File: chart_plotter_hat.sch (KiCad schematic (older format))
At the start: 66 parts, among them J1 JST PH, J10 JST PH, J2 JST PH, J3 40HAT, J4 JST PH, J5 JST PH, J6 JST PH, J7 JST PH, J8 Conn_02x03_Odd_Even, J9 JST PH, Q1 DMG2305UX, Q2 DMMT5401, U1 ATmega328P-AU, U10 DCP01B, U11 VCAN26A2, U2 CAT24C32, U3 MPM3610-5.0-adafruit, U4 LT1762-3.3, U5 G3VM-201FR, U6 MCP2515-xSO, U7 MCP2551-I-SN, U8 LT1762-MS8, U9 ADuM1201BR, Y1 16MHz

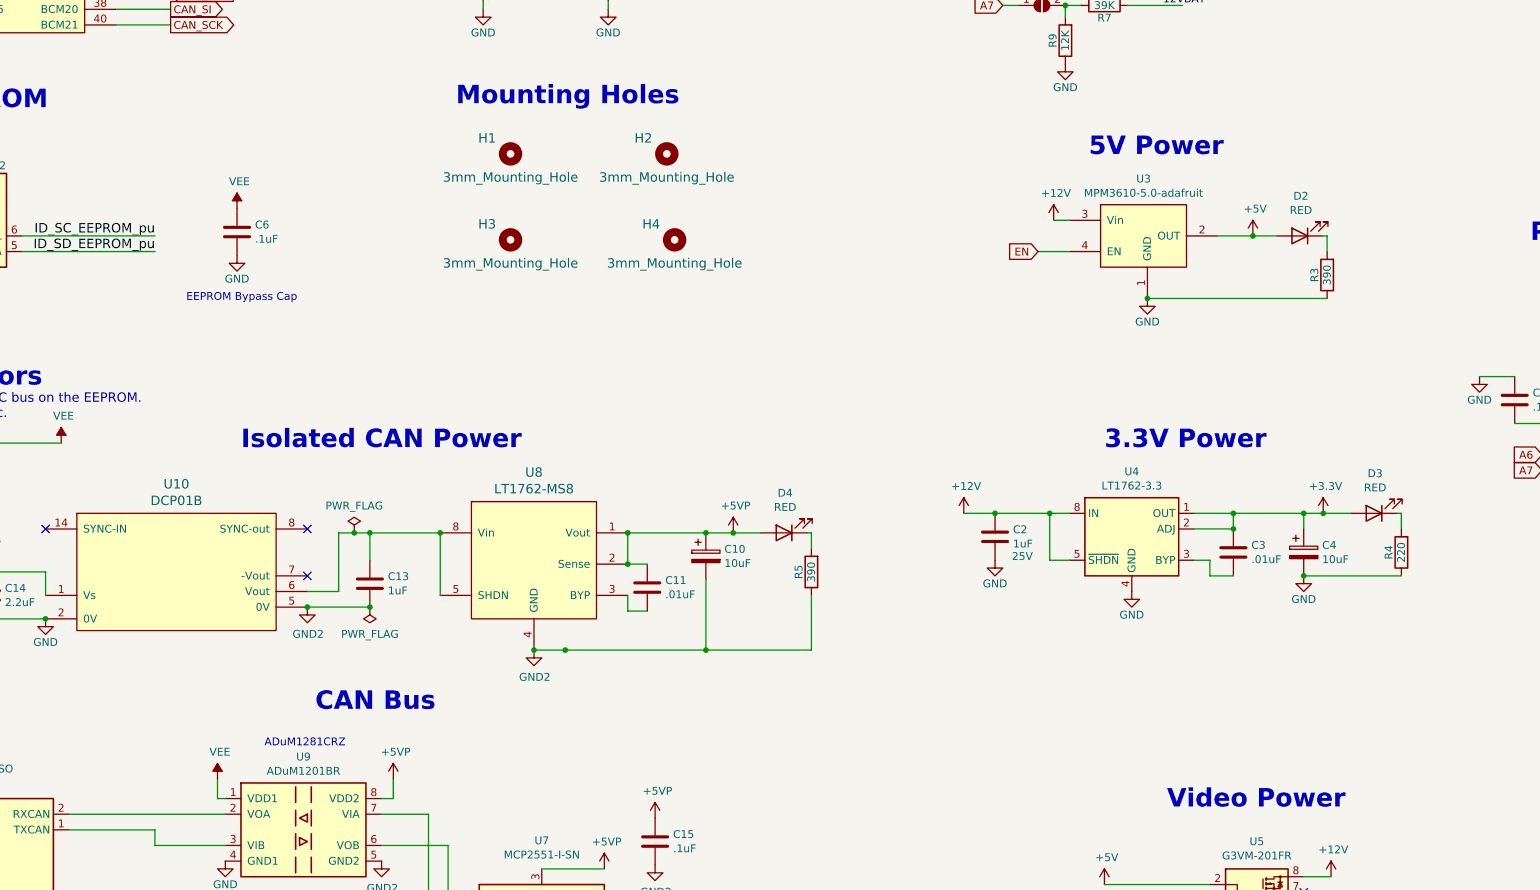
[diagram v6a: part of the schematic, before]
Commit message: Added DS1307 RTC
Added coin cell battery holder
updated bom
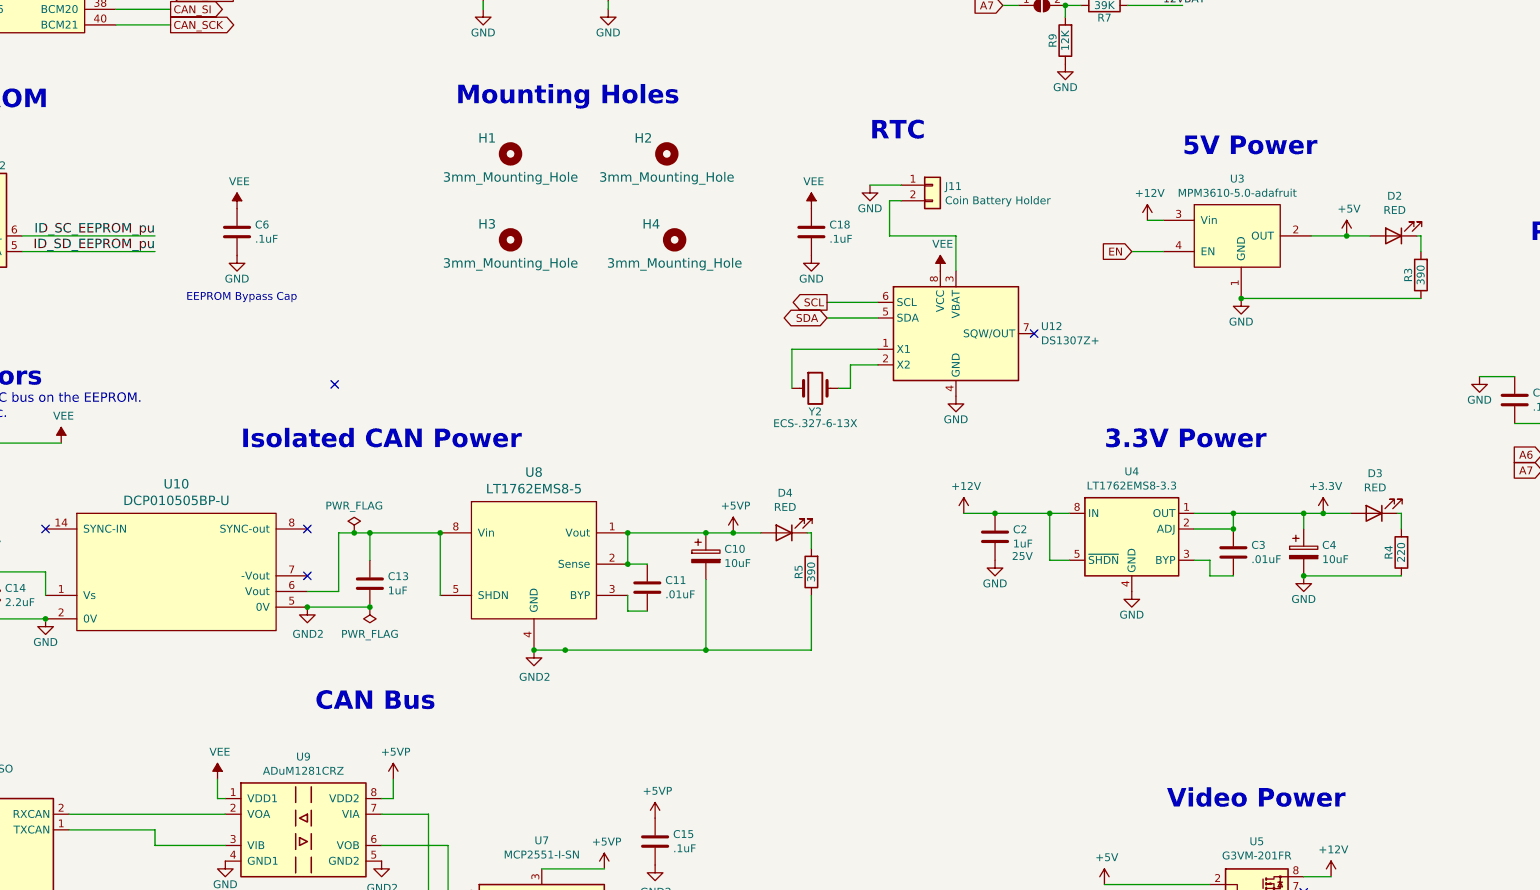
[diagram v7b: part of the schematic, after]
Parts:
- added C18: .1uF, Capacitors_SMD:C_0603, symbol Device:C
- added J11: Coin Battery Holder, geda:3001, symbol Connector_Generic:Conn_01x02
- added U12: DS1307Z+, Housings_SOIC:SOIC-8_3.9x4.9mm_Pitch1.27mm, symbol Timer_RTC:DS1307Z+
- added Y2: ECS-.327-6-13X, Crystals:Crystal_Round_d2.0mm_Vertical, symbol Device:Crystal
- U10: value DCP01B -> DCP010505BP-U
- U4: value LT1762-3.3 -> LT1762EMS8-3.3
- U8: value LT1762-MS8 -> LT1762EMS8-5
- U9: value ADuM1201BR -> ADuM1281CRZ
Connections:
- net GND: now also C18.2, J11.1 (Pin_1), U12.4 (GND)
- net SCL: now also U12.6 (SCL)
- net SDA: now also U12.5 (SDA)
- net VEE: now also C18.1, U12.8 (VCC)
- new net: U12.1 (X1), Y2.1
- new net: U12.2 (X2), Y2.2
- new net: J11.2 (Pin_2), U12.3 (VBAT)
- no-connect marks 25 -> 27
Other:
- note added: "RTC"
- note removed: "ADuM1281CRZ"
- moved on the sheet: D2, R3, U3
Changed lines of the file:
@@
 Power Connector
 Wire Wire Line
-	9250 4425 9350 4425
-Text GLabel 9150 4625 0    50   Input ~ 0
+	9850 4425 9950 4425
+Text GLabel 9750 4625 0    50   Input ~ 0
 EN
 Text GLabel 13950 7825 2    50   Output ~ 0
@@
 L power:+12V #PWR016
 U 1 1 5FDF51C8
-P 9250 4425
-F 0 "#PWR016" H 9250 4275 50  0001 C CNN
-F 1 "+12V" H 9265 4598 50  0000 C CNN
-F 2 "" H 9250 4425 50  0001 C CNN
-F 3 "" H 9250 4425 50  0001 C CNN
-	1    9250 4425
+P 9850 4425
+F 0 "#PWR016" H 9850 4275 50  0001 C CNN
+F 1 "+12V" H 9865 4598 50  0000 C CNN
+F 2 "" H 9850 4425 50  0001 C CNN
+F 3 "" H 9850 4425 50  0001 C CNN
+	1    9850 4425
 	1    0    0    -1
 $EndComp
@@
 P 9750 6500
 F 0 "U4" H 9750 6967 50  0000 C CNN
-F 1 "LT1762-3.3" H 9750 6876 50  0000 C CNN
+F 1 "LT1762EMS8-3.3" H 9750 6876 50  0000 C CNN
 F 2 "Housings_SSOP:MSOP-8_3x3mm_Pitch0.65mm" H 9750 6150 50  0001 C CNN
 F 3 "https://www.analog.com/media/en/technical-documentation/data-sheets/LT1762.pdf" H 9750 5950 50  0001 C CNN
@@
 L power:GND #PWR0105
 U 1 1 5FD9629F
-P 9850 4925
-F 0 "#PWR0105" H 9850 4675 50  0001 C CNN
-F 1 "GND" H 9850 4775 50  0000 C CNN
-F 2 "" H 9850 4925 50  0000 C CNN
-F 3 "" H 9850 4925 50  0000 C CNN
-	1    9850 4925
+P 10450 4925
+F 0 "#PWR0105" H 10450 4675 50  0001 C CNN
+F 1 "GND" H 10450 4775 50  0000 C CNN
+F 2 "" H 10450 4925 50  0000 C CNN
+F 3 "" H 10450 4925 50  0000 C CNN
+	1    10450 4925
 	1    0    0    -1
 $EndComp
@@
 Text Notes 9575 5900 0    118  ~ 24
 3.3V Power
-Text Notes 9475 4025 0    118  ~ 24
+Text Notes 10075 4025 0    118  ~ 24
 5V Power
 Text Notes 12300 4575 0    118  ~ 24
@@
 L adafruit:MPM3610-adafruit U3
 U 1 1 5FD6743F
-P 9850 4275
-F 0 "U3" H 9825 4390 50  0000 C CNN
-F 1 "MPM3610-5.0-adafruit" H 9825 4299 50  0000 C CNN
-F 2 "CustomComponents:Adafruit_MPM3610" H 9850 4275 50  0001 C CNN
-F 3 "" H 9850 4275 50  0001 C CNN
-	1    9850 4275
-	1    0    0    -1
-$EndComp
-Wire Wire Line
-	9150 4625 9350 4625
+P 10450 4275
+F 0 "U3" H 10425 4390 50  0000 C CNN
+F 1 "MPM3610-5.0-adafruit" H 10425 4299 50  0000 C CNN
+F 2 "CustomComponents:Adafruit_MPM3610" H 10450 4275 50  0001 C CNN
+F 3 "" H 10450 4275 50  0001 C CNN
+	1    10450 4275
+	1    0    0    -1
+$EndComp
+Wire Wire Line
+	9750 4625 9950 4625
 $Comp
 L CustomComponents:G3VM-201FR U5
@@
 L power:+5V #PWR0121
 U 1 1 600ECE9F
-P 10525 4525
-F 0 "#PWR0121" H 10525 4375 50  0001 C CNN
-F 1 "+5V" H 10540 4698 50  0000 C CNN
-F 2 "" H 10525 4525 50  0001 C CNN
-F 3 "" H 10525 4525 50  0001 C CNN
-	1    10525 4525
+P 11125 4525
+F 0 "#PWR0121" H 11125 4375 50  0001 C CNN
+F 1 "+5V" H 11140 4698 50  0000 C CNN
+F 2 "" H 11125 4525 50  0001 C CNN
+F 3 "" H 11125 4525 50  0001 C CNN
+	1    11125 4525
 	1    0    0    -1
 $EndComp
@@
 P 4450 8325
 F 0 "U9" H 4450 8792 50  0000 C CNN
-F 1 "ADuM1201BR" H 4450 8701 50  0000 C CNN
+F 1 "ADuM1281CRZ" H 4450 8701 50  0000 C CNN
 F 2 "Housings_SOIC:SOIC-8_3.9x4.9mm_Pitch1.27mm" H 4450 7925 50  0001 C CIN
 F 3 "https://www.analog.com/static/imported-files/data_sheets/ADuM1200_1201.pdf" H 4450 8225 50  0001 C CNN
@@
 	15100 4900 15425 4900
 Wire Wire Line
-	10300 4525 10525 4525
+	10900 4525 11125 4525
 NoConn ~ 15575 1275
 Text GLabel 3275 9425 2    50   Input ~ 0
@@
 P 5925 6625
 F 0 "U8" H 5925 7212 60  0000 C CNN
-F 1 "LT1762-MS8" H 5925 7106 60  0000 C CNN
+F 1 "LT1762EMS8-5" H 5925 7106 60  0000 C CNN
 F 2 "Housings_SSOP:MSOP-8_3x3mm_Pitch0.65mm" H 5925 6625 60  0001 C CNN
 F 3 "" H 5925 6625 60  0001 C CNN
@@
 P 3625 6700
 F 0 "U10" H 3637 7287 60  0000 C CNN
-F 1 "DCP01B" H 3637 7181 60  0000 C CNN
+F 1 "DCP010505BP-U" H 3637 7181 60  0000 C CNN
 F 2 "CustomComponents:DCP01B_SO_7_14" H 3650 6700 60  0001 C CNN
 F 3 "" H 3650 6700 60  0001 C CNN
@@
 L Device:R R3
 U 1 1 616854F3
-P 11000 4775
-F 0 "R3" V 11080 4775 50  0000 C CNN
-F 1 "390" V 11000 4775 50  0000 C CNN
-F 2 "Resistors_SMD:R_0603" V 10930 4775 50  0001 C CNN
-F 3 "" H 11000 4775 50  0001 C CNN
-	1    11000 4775
+P 11600 4775
+F 0 "R3" V 11680 4775 50  0000 C CNN
+F 1 "390" V 11600 4775 50  0000 C CNN
+F 2 "Resistors_SMD:R_0603" V 11530 4775 50  0001 C CNN
+F 3 "" H 11600 4775 50  0001 C CNN
+	1    11600 4775
 	-1   0    0    1
 $EndComp
@@
 L Device:LED D2
 U 1 1 616837C9
-P 10825 4525
-F 0 "D2" H 10818 4270 50  0000 C CNN
-F 1 "RED" H 10818 4361 50  0000 C CNN
-F 2 "Diodes_SMD:D_0603" H 10825 4525 50  0001 C CNN
-F 3 "~" H 10825 4525 50  0001 C CNN
-	1    10825 4525
+P 11425 4525
+F 0 "D2" H 11418 4270 50  0000 C CNN
+F 1 "RED" H 11418 4361 50  0000 C CNN
+F 2 "Diodes_SMD:D_0603" H 11425 4525 50  0001 C CNN
+F 3 "~" H 11425 4525 50  0001 C CNN
+	1    11425 4525
 	-1   0    0    1
 $EndComp
@@
 $EndComp
 Wire Wire Line
-	10525 4525 10675 4525
-Connection ~ 10525 4525
-Wire Wire Line
-	10975 4525 11000 4525
-Wire Wire Line
-	11000 4525 11000 4625
-Wire Wire Line
-	11000 4925 9850 4925
-Connection ~ 9850 4925
+	11125 4525 11275 4525
+Connection ~ 11125 4525
+Wire Wire Line
+	11575 4525 11600 4525
+Wire Wire Line
+	11600 4525 11600 4625
+Wire Wire Line
+	11600 4925 10450 4925
+Connection ~ 10450 4925
 Wire Wire Line
 	10975 6300 11150 6300
@@
 Wire Wire Line
 	1600 8425 1750 8425
-Text Notes 4200 7800 0    50   ~ 0
-ADuM1281CRZ
 Connection ~ 2425 6675
 Connection ~ 6125 7175
@@
 	6125 7175 7025 7175
 Connection ~ 5925 7175
+$Comp
+L Timer_RTC:DS1307Z+ U12
+U 1 1 6144E9CC
+P 8625 5150
+F 0 "U12" H 9169 5196 50  0000 L CNN
+F 1 "DS1307Z+" H 9169 5105 50  0000 L CNN
+F 2 "Housings_SOIC:SOIC-8_3.9x4.9mm_Pitch1.27mm" H 8625 4650 50  0001 C CNN
+F 3 "https://datasheets.maximintegrated.com/en/ds/DS1307.pdf" H 8625 5150 50  0001 C CNN
+	1    8625 5150
+	1    0    0    -1
+$EndComp
+Wire Wire Line
+	8125 4950 7800 4950
+Wire Wire Line
+	8125 5050 7800 5050
+$Comp
+L power:VEE #PWR037
+U 1 1 6149D61D
+P 8525 4750
+F 0 "#PWR037" H 8525 4600 50  0001 C CNN
+F 1 "VEE" H 8540 4923 50  0000 C CNN
+F 2 "" H 8525 4750 50  0001 C CNN
+F 3 "" H 8525 4750 50  0001 C CNN
+	1    8525 4750
+	1    0    0    -1
+$EndComp
+$Comp
+L power:GND #PWR038
+U 1 1 614A02FA
+P 8625 5550
+F 0 "#PWR038" H 8625 5300 50  0001 C CNN
+F 1 "GND" H 8625 5400 50  0000 C CNN
+F 2 "" H 8625 5550 50  0000 C CNN
+F 3 "" H 8625 5550 50  0000 C CNN
+	1    8625 5550
+	1    0    0    -1
+$EndComp
+$Comp
+L Connector_Generic:Conn_01x02 J11
+U 1 1 614A429A
+P 8475 4200
+F 0 "J11" H 8555 4192 50  0000 L CNN
+F 1 "Coin Battery Holder" H 8555 4101 50  0000 L CNN
+F 2 "geda:3001" H 8475 4200 50  0001 C CNN
+F 3 "~" H 8475 4200 50  0001 C CNN
+	1    8475 4200
+	1    0    0    -1
+$EndComp
+$Comp
+L power:GND #PWR036
+U 1 1 614F655A
+P 8075 4200
+F 0 "#PWR036" H 8075 3950 50  0001 C CNN
+F 1 "GND" H 8075 4050 50  0000 C CNN
+F 2 "" H 8075 4200 50  0000 C CNN
+F 3 "" H 8075 4200 50  0000 C CNN
+	1    8075 4200
+	1    0    0    -1
+$EndComp
+Wire Wire Line
+	8625 4525 8625 4750
+$Comp
+L Device:Crystal Y2
+U 1 1 6150DAC1
+P 7725 5500
+F 0 "Y2" H 7725 5350 50  0000 C CNN
+F 1 "ECS-.327-6-13X" H 7725 5275 50  0000 C CNN
+F 2 "Crystals:Crystal_Round_d2.0mm_Vertical" H 7725 5500 50  0001 C CNN
+F 3 "~" H 7725 5500 50  0001 C CNN
+	1    7725 5500
+	1    0    0    -1
+$EndComp
+Wire Wire Line
+	7875 5500 7950 5500
+Wire Wire Line
+	7950 5500 7950 5350
+Wire Wire Line
+	7950 5350 8125 5350
+Wire Wire Line
+	7575 5500 7575 5250
+NoConn ~ 9125 5150
+NoConn ~ 4650 5475
+Text GLabel 7800 5050 0    50   BiDi ~ 0
+SDA
+Text GLabel 7800 4950 0    50   Output ~ 0
+SCL
+Wire Wire Line
+	7575 5250 8125 5250
+Wire Wire Line
+	8075 4200 8275 4200
+Wire Wire Line
+	8625 4525 8200 4525
+Wire Wire Line
+	8200 4525 8200 4300
+Wire Wire Line
+	8200 4300 8275 4300
+$Comp
+L Device:C C18
+U 1 1 614B5FFD
+P 7700 4500
+F 0 "C18" H 7815 4546 50  0000 L CNN
+F 1 ".1uF" H 7815 4455 50  0000 L CNN
+F 2 "Capacitors_SMD:C_0603" H 7738 4350 50  0001 C CNN
+F 3 "~" H 7700 4500 50  0001 C CNN
+	1    7700 4500
+	1    0    0    -1
+$EndComp
+$Comp
+L power:GND #PWR042
+U 1 1 614D209C
+P 7700 4650
+F 0 "#PWR042" H 7700 4400 50  0001 C CNN
+F 1 "GND" H 7700 4500 50  0000 C CNN
+F 2 "" H 7700 4650 50  0000 C CNN
+F 3 "" H 7700 4650 50  0000 C CNN
+	1    7700 4650
+	1    0    0    -1
+$EndComp
+$Comp
+L power:VEE #PWR0110
+U 1 1 6151C438
+P 7700 4350
+F 0 "#PWR0110" H 7700 4200 50  0001 C CNN
+F 1 "VEE" H 7715 4523 50  0000 C CNN
+F 2 "" H 7700 4350 50  0001 C CNN
+F 3 "" H 7700 4350 50  0001 C CNN
+	1    7700 4350
+	1    0    0    -1
+$EndComp
+Text Notes 8075 3925 0    118  ~ 24
+RTC
 $EndSCHEMATC

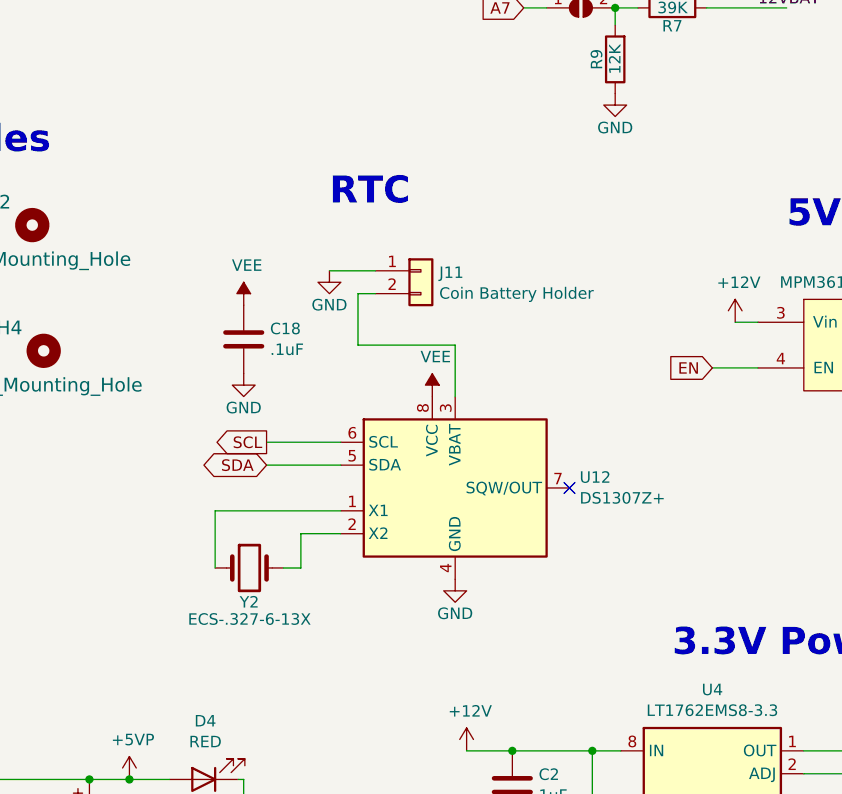
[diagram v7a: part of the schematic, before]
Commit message: Removed DS1307, (Not avail), added STEMMA QT conx
can connect an adafruit breakout board for RTC instead
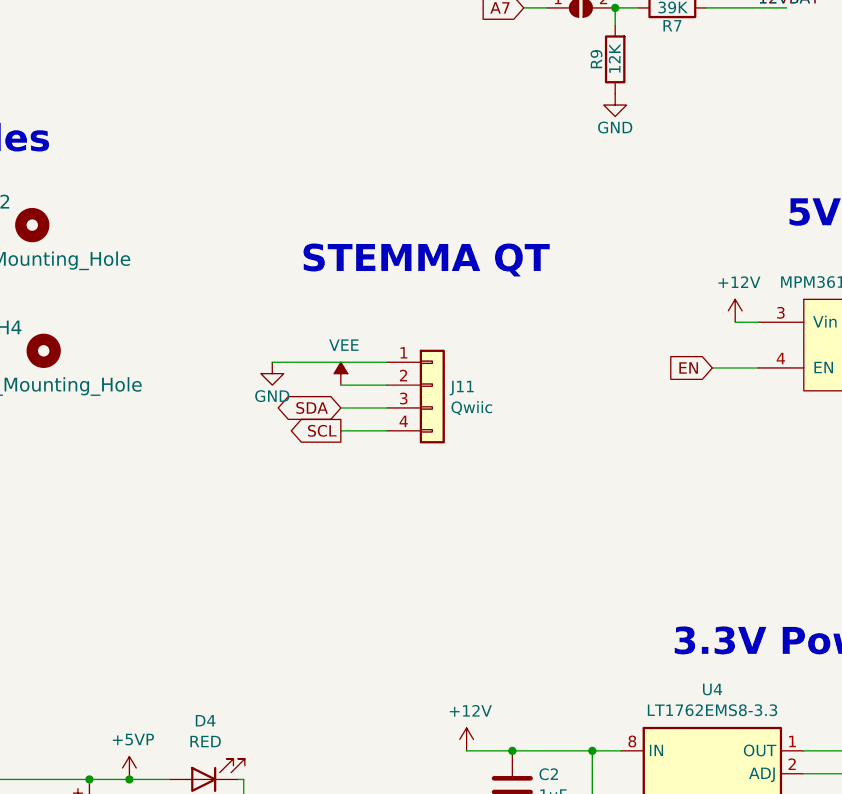
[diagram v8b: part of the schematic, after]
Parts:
- removed C18: .1uF, Capacitors_SMD:C_0603, symbol Device:C
- removed J11: Coin Battery Holder, geda:3001, symbol Connector_Generic:Conn_01x02
- removed U12: DS1307Z+, Housings_SOIC:SOIC-8_3.9x4.9mm_Pitch1.27mm, symbol Timer_RTC:DS1307Z+
- removed Y2: ECS-.327-6-13X, Crystals:Crystal_Round_d2.0mm_Vertical, symbol Device:Crystal
- added J11: Qwiic, Connectors_JST:JST_SH_BM04B-SRSS-TB_04x1.00mm_Straight, symbol Connector_Generic:Conn_01x04
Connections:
- net GND: now also J11.1 (Pin_1)
- net SCL: now also J11.4 (Pin_4)
- net SDA: now also J11.3 (Pin_3)
- net VEE: now also J11.2 (Pin_2)
- no-connect marks 27 -> 26
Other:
- note added: "STEMMA QT"
- note removed: "RTC"
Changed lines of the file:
@@
 	6125 7175 7025 7175
 Connection ~ 5925 7175
-$Comp
-L Timer_RTC:DS1307Z+ U12
-U 1 1 6144E9CC
-P 8625 5150
-F 0 "U12" H 9169 5196 50  0000 L CNN
-F 1 "DS1307Z+" H 9169 5105 50  0000 L CNN
-F 2 "Housings_SOIC:SOIC-8_3.9x4.9mm_Pitch1.27mm" H 8625 4650 50  0001 C CNN
-F 3 "https://datasheets.maximintegrated.com/en/ds/DS1307.pdf" H 8625 5150 50  0001 C CNN
-	1    8625 5150
-	1    0    0    -1
-$EndComp
-Wire Wire Line
-	8125 4950 7800 4950
-Wire Wire Line
-	8125 5050 7800 5050
-$Comp
-L power:VEE #PWR037
-U 1 1 6149D61D
-P 8525 4750
-F 0 "#PWR037" H 8525 4600 50  0001 C CNN
-F 1 "VEE" H 8540 4923 50  0000 C CNN
-F 2 "" H 8525 4750 50  0001 C CNN
-F 3 "" H 8525 4750 50  0001 C CNN
-	1    8525 4750
-	1    0    0    -1
-$EndComp
-$Comp
-L power:GND #PWR038
-U 1 1 614A02FA
-P 8625 5550
-F 0 "#PWR038" H 8625 5300 50  0001 C CNN
-F 1 "GND" H 8625 5400 50  0000 C CNN
-F 2 "" H 8625 5550 50  0000 C CNN
-F 3 "" H 8625 5550 50  0000 C CNN
-	1    8625 5550
-	1    0    0    -1
-$EndComp
-$Comp
-L Connector_Generic:Conn_01x02 J11
-U 1 1 614A429A
-P 8475 4200
-F 0 "J11" H 8555 4192 50  0000 L CNN
-F 1 "Coin Battery Holder" H 8555 4101 50  0000 L CNN
-F 2 "geda:3001" H 8475 4200 50  0001 C CNN
-F 3 "~" H 8475 4200 50  0001 C CNN
-	1    8475 4200
-	1    0    0    -1
-$EndComp
-$Comp
-L power:GND #PWR036
-U 1 1 614F655A
-P 8075 4200
-F 0 "#PWR036" H 8075 3950 50  0001 C CNN
-F 1 "GND" H 8075 4050 50  0000 C CNN
-F 2 "" H 8075 4200 50  0000 C CNN
-F 3 "" H 8075 4200 50  0000 C CNN
-	1    8075 4200
-	1    0    0    -1
-$EndComp
-Wire Wire Line
-	8625 4525 8625 4750
-$Comp
-L Device:Crystal Y2
-U 1 1 6150DAC1
-P 7725 5500
-F 0 "Y2" H 7725 5350 50  0000 C CNN
-F 1 "ECS-.327-6-13X" H 7725 5275 50  0000 C CNN
-F 2 "Crystals:Crystal_Round_d2.0mm_Vertical" H 7725 5500 50  0001 C CNN
-F 3 "~" H 7725 5500 50  0001 C CNN
-	1    7725 5500
-	1    0    0    -1
-$EndComp
-Wire Wire Line
-	7875 5500 7950 5500
-Wire Wire Line
-	7950 5500 7950 5350
-Wire Wire Line
-	7950 5350 8125 5350
-Wire Wire Line
-	7575 5500 7575 5250
-NoConn ~ 9125 5150
 NoConn ~ 4650 5475
-Text GLabel 7800 5050 0    50   BiDi ~ 0
+Text GLabel 8125 4800 0    50   BiDi ~ 0
 SDA
-Text GLabel 7800 4950 0    50   Output ~ 0
+Text GLabel 8125 4900 0    50   Output ~ 0
 SCL
-Wire Wire Line
-	7575 5250 8125 5250
-Wire Wire Line
-	8075 4200 8275 4200
-Wire Wire Line
-	8625 4525 8200 4525
-Wire Wire Line
-	8200 4525 8200 4300
-Wire Wire Line
-	8200 4300 8275 4300
-$Comp
-L Device:C C18
-U 1 1 614B5FFD
-P 7700 4500
-F 0 "C18" H 7815 4546 50  0000 L CNN
-F 1 ".1uF" H 7815 4455 50  0000 L CNN
-F 2 "Capacitors_SMD:C_0603" H 7738 4350 50  0001 C CNN
-F 3 "~" H 7700 4500 50  0001 C CNN
-	1    7700 4500
-	1    0    0    -1
-$EndComp
 $Comp
 L power:GND #PWR042
 U 1 1 614D209C
-P 7700 4650
-F 0 "#PWR042" H 7700 4400 50  0001 C CNN
-F 1 "GND" H 7700 4500 50  0000 C CNN
-F 2 "" H 7700 4650 50  0000 C CNN
-F 3 "" H 7700 4650 50  0000 C CNN
-	1    7700 4650
+P 7825 4600
+F 0 "#PWR042" H 7825 4350 50  0001 C CNN
+F 1 "GND" H 7825 4450 50  0000 C CNN
+F 2 "" H 7825 4600 50  0000 C CNN
+F 3 "" H 7825 4600 50  0000 C CNN
+	1    7825 4600
 	1    0    0    -1
 $EndComp
@@
 L power:VEE #PWR0110
 U 1 1 6151C438
-P 7700 4350
-F 0 "#PWR0110" H 7700 4200 50  0001 C CNN
-F 1 "VEE" H 7715 4523 50  0000 C CNN
-F 2 "" H 7700 4350 50  0001 C CNN
-F 3 "" H 7700 4350 50  0001 C CNN
-	1    7700 4350
+P 8125 4700
+F 0 "#PWR0110" H 8125 4550 50  0001 C CNN
+F 1 "VEE" H 8140 4873 50  0000 C CNN
+F 2 "" H 8125 4700 50  0001 C CNN
+F 3 "" H 8125 4700 50  0001 C CNN
+	1    8125 4700
 	1    0    0    -1
 $EndComp
-Text Notes 8075 3925 0    118  ~ 24
-RTC
+Text Notes 7950 4225 0    118  ~ 24
+STEMMA QT
+$Comp
+L Connector_Generic:Conn_01x04 J11
+U 1 1 615837CF
+P 8525 4700
+F 0 "J11" H 8605 4692 50  0000 L CNN
+F 1 "Qwiic" H 8605 4601 50  0000 L CNN
+F 2 "Connectors_JST:JST_SH_BM04B-SRSS-TB_04x1.00mm_Straight" H 8525 4700 50  0001 C CNN
+F 3 "~" H 8525 4700 50  0001 C CNN
+	1    8525 4700
+	1    0    0    -1
+$EndComp
+Wire Wire Line
+	8325 4900 8125 4900
+Wire Wire Line
+	8325 4800 8125 4800
+Wire Wire Line
+	8325 4700 8125 4700
+Wire Wire Line
+	8325 4600 7825 4600
 $EndSCHEMATC
